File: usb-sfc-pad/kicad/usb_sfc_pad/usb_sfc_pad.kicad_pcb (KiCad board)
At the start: 2 copper layers, 125.7 x 61.8 mm, 36 parts, among them IC101 PIC16F1459-ISS, J101 532610571, J102 HEADER_6P-2.54, J103 533980271, J104 533980271, J105 533980271, J106 533980271, SW101 SW_Pad, SW102 SW_Pad, SW103 SW_Pad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

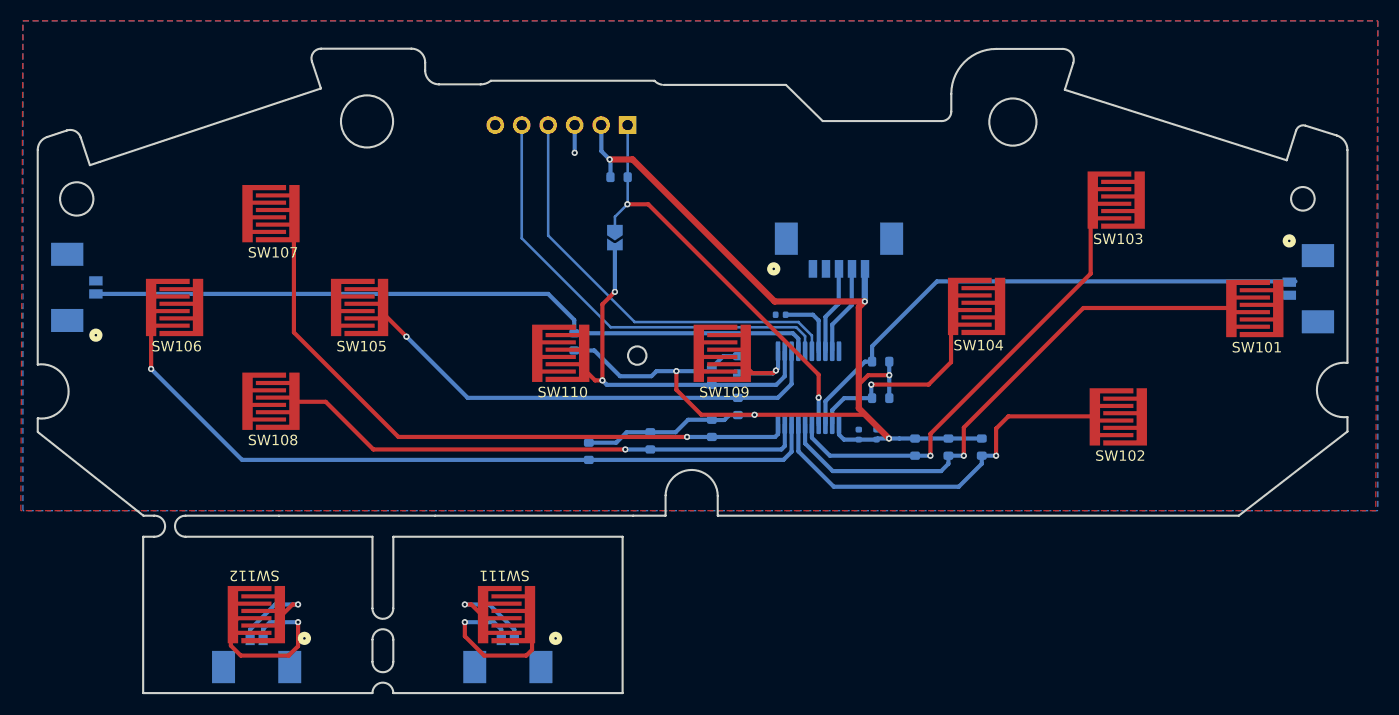
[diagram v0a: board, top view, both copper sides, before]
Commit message: Fix LR connectors' placement
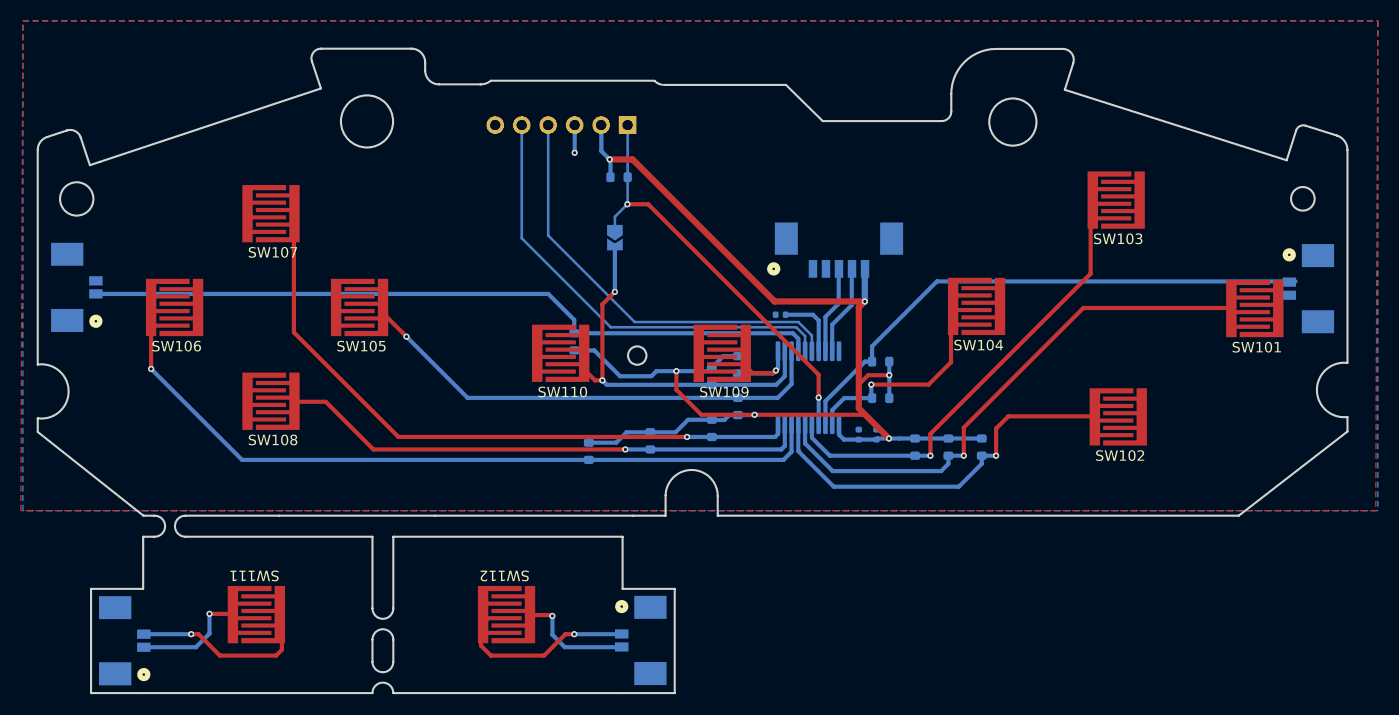
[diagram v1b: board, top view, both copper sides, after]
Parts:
- moved J106 37.1 mm to (149.4, 139.4), turned to 90 degrees
- moved J104 37.0 mm to (99.6, 139.5), turned to -90 degrees
- moved SW111 24.0 mm to (112.4, 137.0)
- moved SW112 24.0 mm to (136.4, 137.0)
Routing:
- net Net-(J106-Pad2): track 8.42 -> 10.9 mm
- net Net-(J104-Pad1): track 8.52 -> 10.8 mm
- net Net-(J104-Pad2): track 17.4 -> 18.3 mm
- net Net-(J106-Pad1): track 18.4 -> 19.0 mm
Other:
- outline, holes or cut-outs redrawn
